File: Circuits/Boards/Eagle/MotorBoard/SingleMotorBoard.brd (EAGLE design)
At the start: 127 x 101.3 mm, 94 parts, among them M1 IRFS7537PBF, M2 IRFS7537PBF, M3 IRFS7537PBF, M4 IRFS7537PBF, M5 IRFS7537PBF, M6 IRFS7537PBF, M7 IRFS7537PBF, M8 IRFS7537PBF, Q1 2N3904, Q10 2N3904, Q11 2N3904, Q12 2N3904, Q13 2N3904, Q14 2N3904, Q15 2N3904, Q16 2N3904, Q2 2N3904, Q3 2N3904, Q4 2N3904, Q5 2N3904, Q6 2N3904, Q7 2N3904, Q8 2N3904, Q9 2N3904

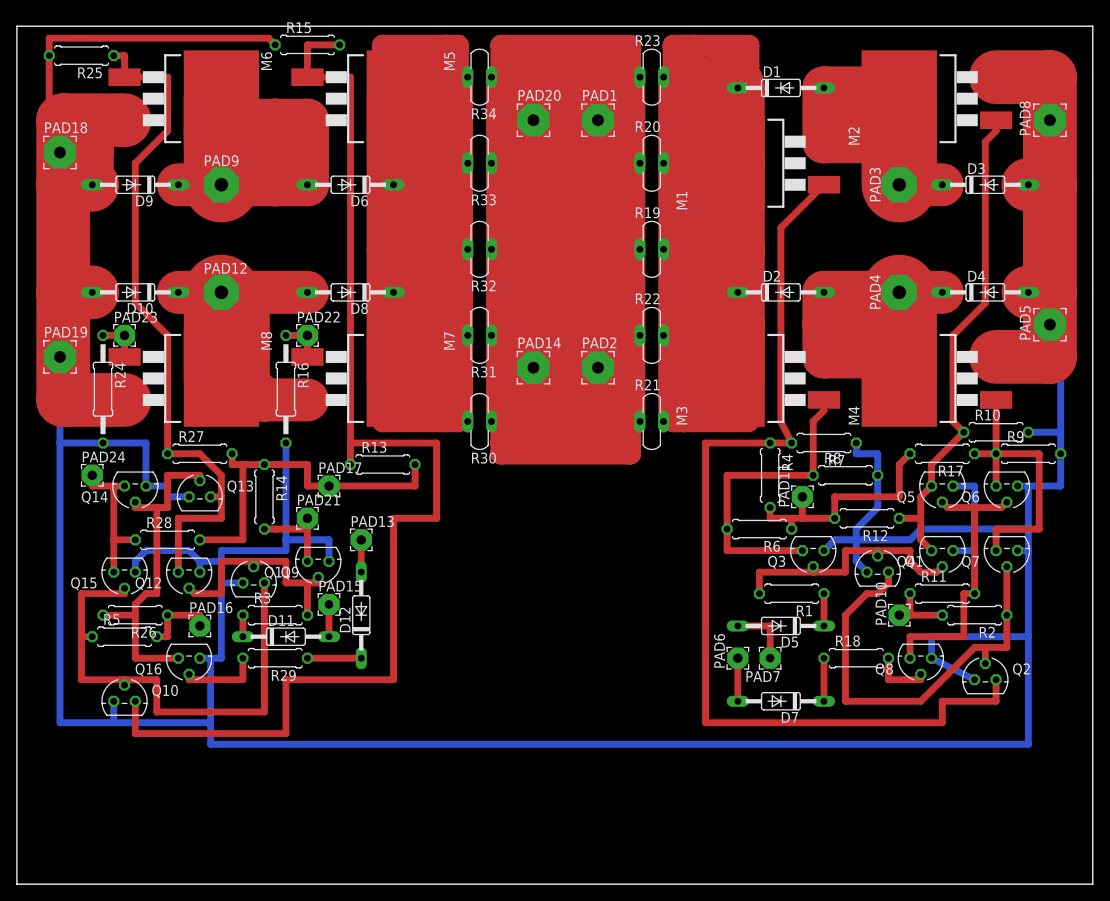
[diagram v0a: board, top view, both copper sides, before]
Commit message: Started moving from EAGLE to KiCAD
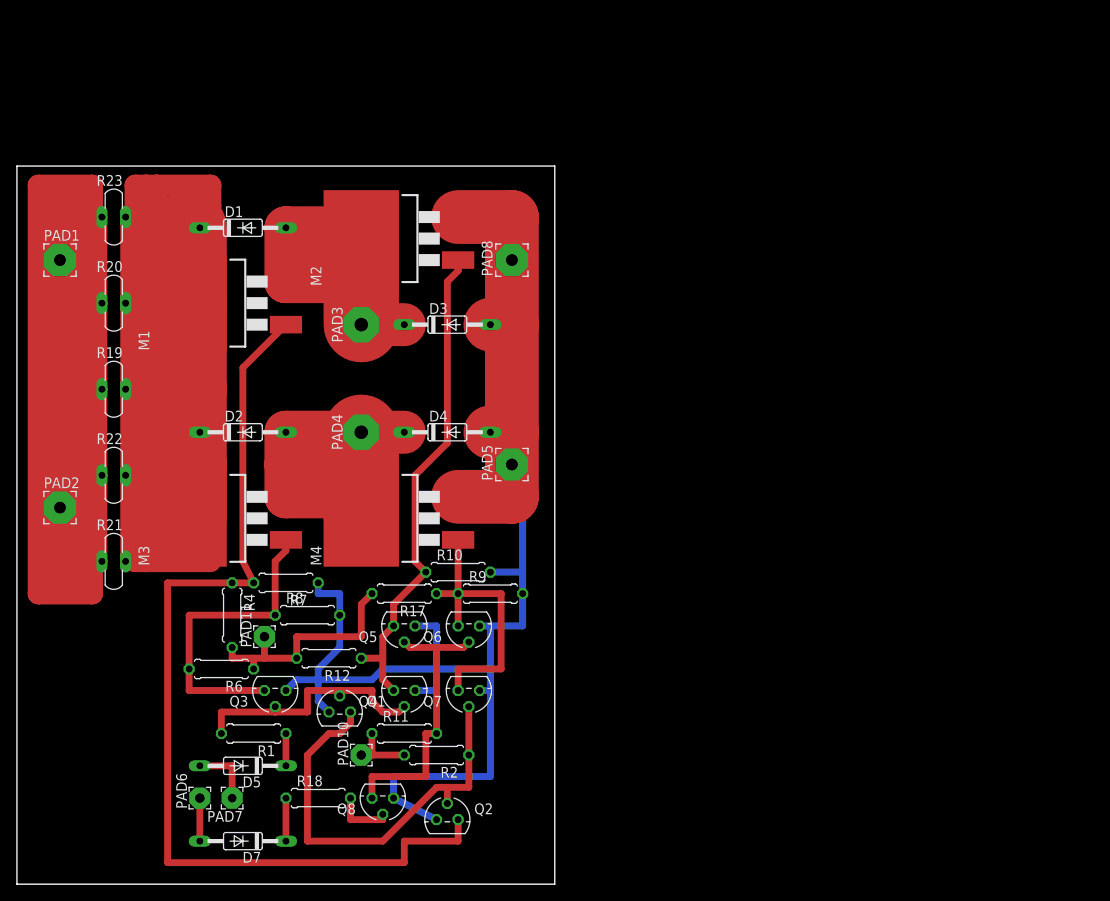
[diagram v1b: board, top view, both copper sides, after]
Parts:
- removed D10, D11, D12, D6, D8, D9: 1N4148DO35-10, diode:DO35-10
- removed M5, M6, M7, M8: IRFS7537PBF, EagleCAD:D2PACK
- removed PAD12, PAD9: WIREPAD4,16O1,6, wirepad:4,16O1,6
- removed PAD13, PAD16, PAD17, PAD21, PAD22, PAD23, PAD24: (no value), wirepad:2,54/1,1
- removed PAD14, PAD18, PAD19, PAD20: (no value), wirepad:3,81/1,4
- removed PAD15: (no value), wirepad:2,54/1,0
- removed Q10, Q11, Q12, Q13, Q14, Q15, Q16, Q9: 2N3904, transistor-npn:TO92
- removed R13, R26, R27, R29, R3, R5: (no value), rcl:0207/7
- removed R14, R15, R25, R28: (no value), resistor:0207/7
- removed R16, R24: (no value), resistor:0207/12
- removed R30, R31, R32, R33, R34: (no value), ptc-ntc:P660A
- moved D1 65.6 mm to (26.7, 77.5)
- moved D2 65.6 mm to (26.7, 53.3)
- moved D3 65.6 mm to (50.8, 66.0)
- moved D4 65.6 mm to (50.8, 53.3)
- moved D5 65.6 mm to (26.7, 14.0)
- moved D7 65.6 mm to (26.7, 5.08)
- moved M1 65.6 mm to (22.9, 68.6)
- moved M2 65.6 mm to (43.2, 76.2)
- moved M3 65.6 mm to (22.9, 43.2)
- moved M4 65.6 mm to (43.2, 43.2)
- moved PAD1 65.6 mm to (5.08, 73.7)
- moved PAD10 65.6 mm to (40.6, 15.2)
- moved PAD2 65.6 mm to (5.08, 44.5)
- moved PAD3 65.6 mm to (40.6, 66.0)
- moved PAD4 65.6 mm to (40.6, 53.3)
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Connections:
- removed net BB1: Q11.2, Q12.2, Q9.2, R3.2
- removed net BFF: PAD21.1, Q11.1, R14.2
- removed net BFG: M7.1, PAD22.1, R16.1
- removed net DIR1: D11.A, PAD15.1
- removed net FB1: Q10.2, Q15.2, Q9.1, R5.1
- removed net FF1: M5.1, Q10.1, R13.1, R15.2
- removed net MN1: D10.C, D8.A, M7.3, M8.2, PAD12.1
- removed net MP1: D6.A, D9.C, M5.3, M6.2, PAD9.1
- removed net N$1: M8.1, PAD23.1, R24.1
- removed net N$10: D12.C, R29.1
- removed net N$11: D12.A, PAD13.1
- removed net N$3: M6.1, Q12.1, Q13.1, R25.1, R27.1
- removed net N$5: PAD24.1, Q14.1, Q15.1, R28.1
- removed net N$6: Q13.2, Q14.2, Q16.1, R26.2
- removed net N$7: Q16.2, R29.2
- removed net N$8: D11.C, R3.1
- removed net VDD1: D6.C, D8.C, M5.2, M7.2, R30.2, R31.2, R32.2, R33.2, R34.2
- removed net VG1: PAD17.1, R13.2, R14.1, R27.2, R28.2
- removed net VSW1: PAD16.1, R26.1, R5.2
- net 0: no longer D10.A, D9.A, M6.3, M8.3, PAD18.1, PAD19.1, Q10.3, Q11.3, Q12.3, Q13.3, Q14.3, Q15.3, Q16.3, Q9.3, R15.1, R16.2, R24.2, R25.2
- net VBAT: no longer PAD14.1, PAD20.1, R30.1, R31.1, R32.1, R33.1, R34.1
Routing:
- net 0: track 541.6 -> 184.8 mm
- net VDD1: track 250.3 -> 0.00 mm
- net VBAT: track 422.5 -> 221.8 mm
- net FF1: track 142.2 -> 0.00 mm
- net N$3: track 81.7 -> 0.00 mm
- net FB1: track 58.4 -> 0.00 mm
- net MN1: track 55.7 -> 0.00 mm
- net MP1: track 51.3 -> 0.00 mm
- net VG1: track 41.9 -> 0.00 mm
- net N$6: track 41.2 -> 0.00 mm
- net BB1: track 26.9 -> 0.00 mm
- net N$5: track 17.8 -> 0.00 mm
- net BFF: track 10.2 -> 0.00 mm
- net N$7: track 9.53 -> 0.00 mm
- net VSW1: track 8.89 -> 0.00 mm
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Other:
- board size 127 x 101.3 mm -> 63.5 x 84.8 mm
